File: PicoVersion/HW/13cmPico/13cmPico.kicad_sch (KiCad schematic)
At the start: 70 parts, among them SW1 KEY_1, SW101 RotaryEncoder_Switch, SW102 RESET, SW2 KEY_2, SW3 KEY_3, U1 ADF4351, U101 Pico, U102 LM4562, U103 LM4562, U104 AD8346, U105 LM4562, U2 KT2520K-T

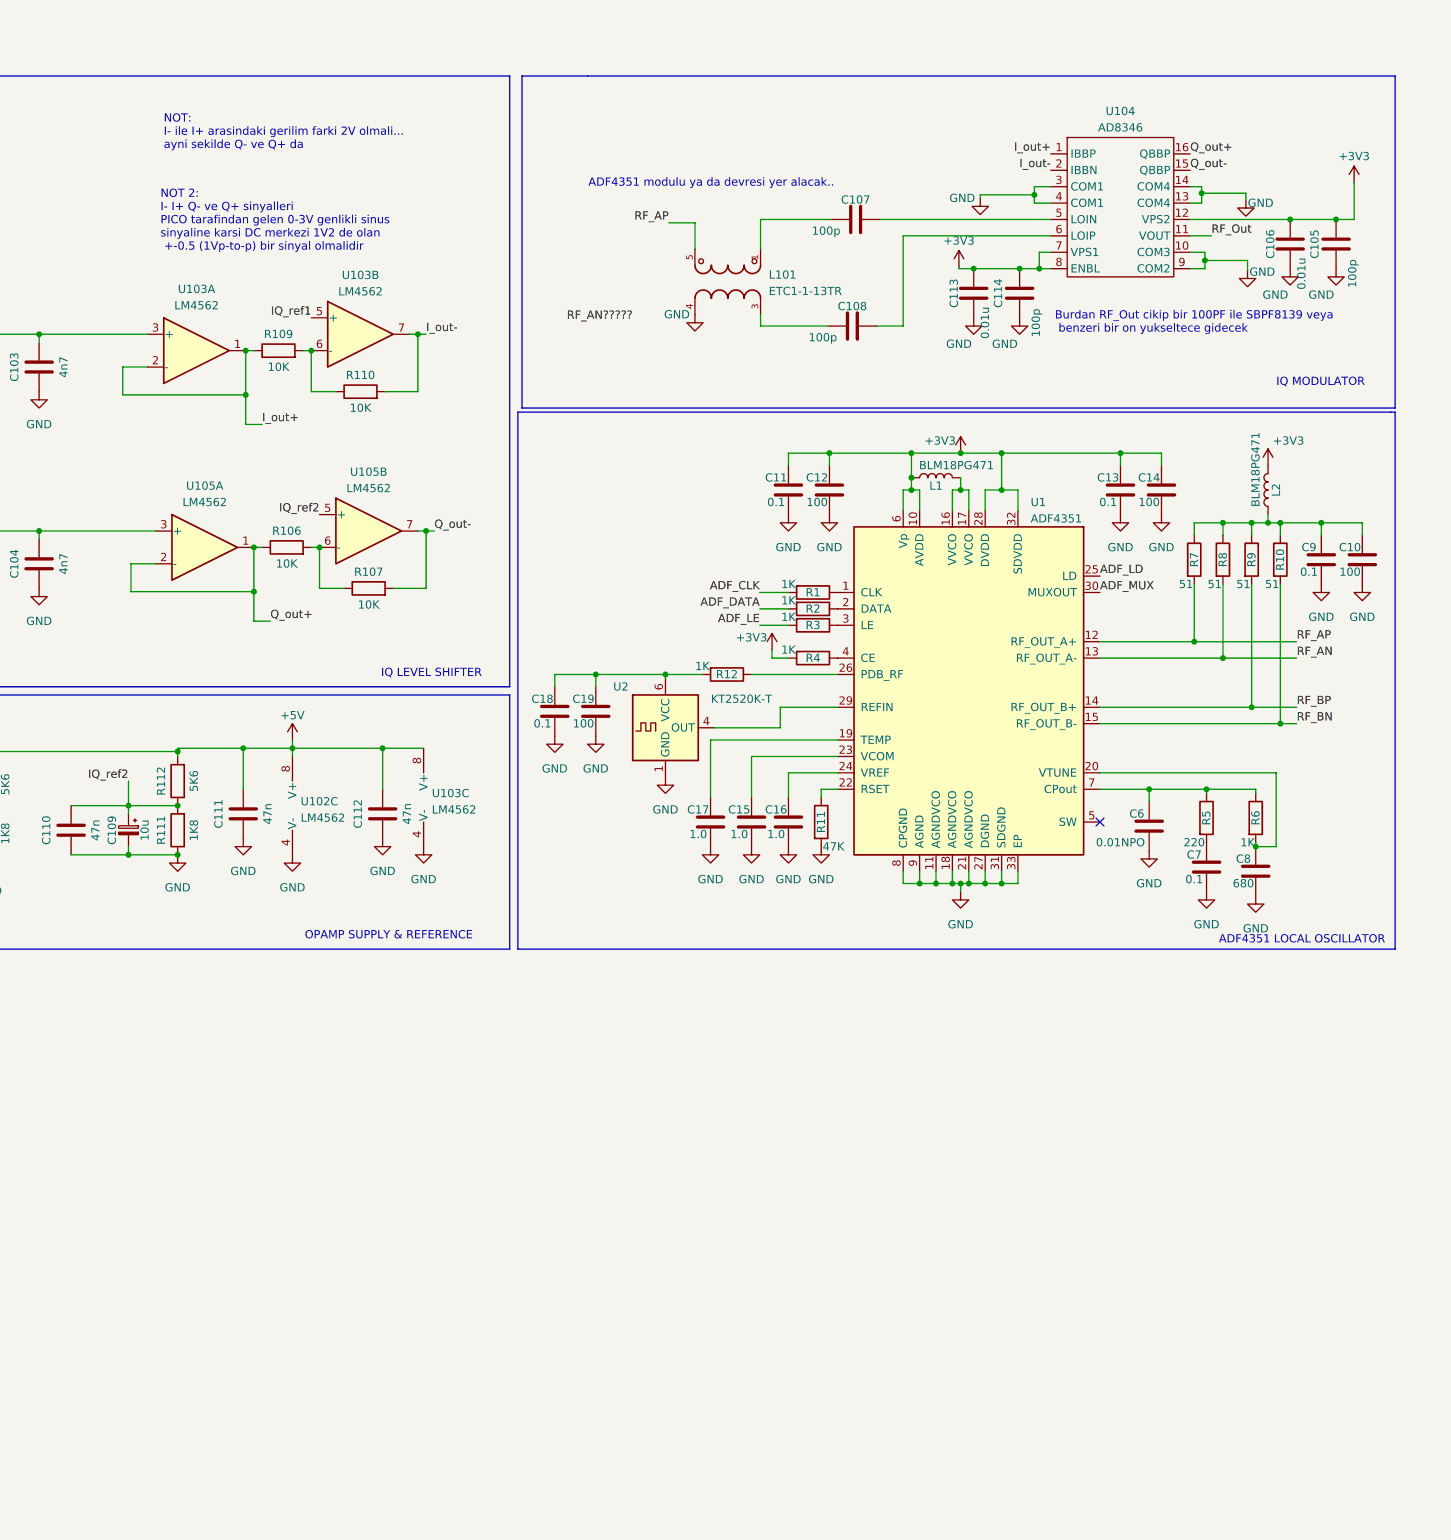
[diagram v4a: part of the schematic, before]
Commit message: ADF435X modules added
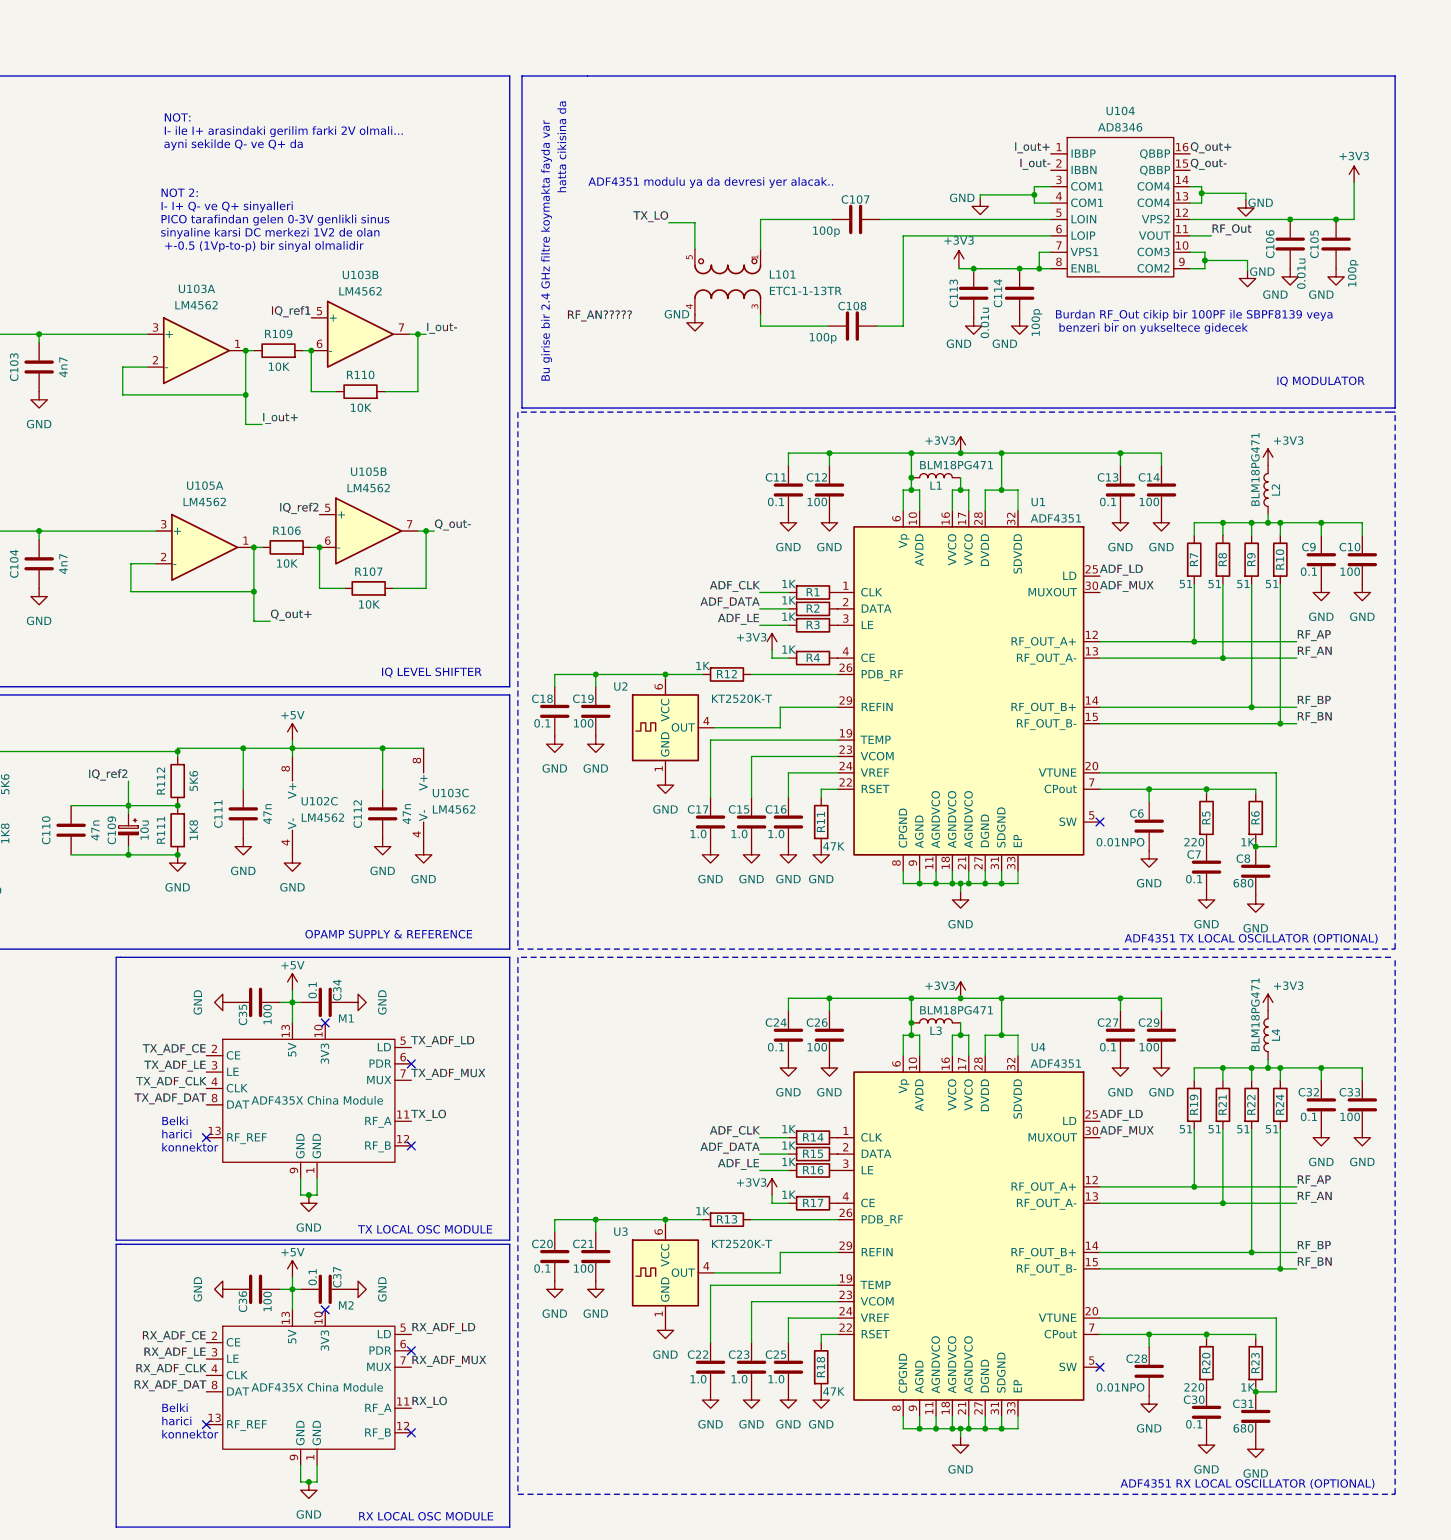
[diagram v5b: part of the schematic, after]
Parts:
- added C20, C24, C27, C30, C32, C34, C37: 0.1, Capacitor_SMD:C_0805_2012Metric, symbol Device:C
- added C21, C26, C29, C33, C35, C36: 100, Capacitor_SMD:C_0805_2012Metric, symbol Device:C
- added C22, C23, C25: 1.0, Capacitor_SMD:C_0805_2012Metric, symbol Device:C
- added C28: 0.01NPO, Capacitor_SMD:C_0805_2012Metric, symbol Device:C
- added C31: 680, Capacitor_SMD:C_0805_2012Metric, symbol Device:C
- added L3, L4: BLM18PG471, symbol Device:L
- added M1, M2: ADF435X China Module, symbol ADF435X_module:ADF435X_China_Module
- added R13, R14, R15, R16, R17, R23: 1K, Resistor_SMD:R_0805_2012Metric, symbol Device:R
- added R18: 47K, Resistor_SMD:R_0805_2012Metric, symbol Device:R
- added R19, R21, R22, R24: 51, Resistor_SMD:R_0805_2012Metric, symbol Device:R
- added R20: 220, Resistor_SMD:R_0805_2012Metric, symbol Device:R
- added U3: KT2520K-T, Oscillator:Oscillator_SMD_Kyocera_2520-6Pin_2.5x2.0mm, symbol Oscillator:KT2520K-T
- added U4: ADF4351, Package_CSP:LFCSP-32-1EP_5x5mm_P0.5mm_EP3.25x3.25mm, symbol Timer_PLL:ADF4351
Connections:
- net +3V3: now also C24.2, C26.2, C27.2, C29.2, L3.1, L4.2, R17.2, U4.10 (AVDD), U4.28 (DVDD), U4.32 (SDVDD), U4.6 (Vp)
- net +5V: now also C34.1, C35.1, C36.1, C37.1, M1.13 (RF_REF), M2.13 (RF_REF)
- net ADF_CLK: now also R14.2
- net ADF_DATA: now also R15.2
- net ADF_LD: now also U4.25 (LD)
- net ADF_LE: now also R16.2
- net ADF_MUX: now also U4.30 (MUXOUT)
- net GND: now also C20.1, C21.1, C22.1, C23.1, C24.1, C25.1, C26.1, C27.1, C28.1, C29.1, C30.1, C31.1, C32.1, C33.1, C34.2, C35.2, C36.2, C37.2, M1.1 (GND), M1.9 (GND), M2.1 (GND), M2.9 (GND), R18.2, U3.1 (GND), U3.3 (GND), U4.11 (AGNDVCO), U4.18 (AGNDVCO), U4.21 (AGNDVCO), U4.27 (DGND), U4.31 (SDGND), U4.33 (EP), U4.8 (CPGND), U4.9 (AGND)
- net RF_AN: now also R21.2, U4.13 (RF_OUT_A-)
- net RF_AP: now also R19.2, U4.12 (RF_OUT_A+); no longer L101.5
- net RF_BN: now also R24.2, U4.15 (RF_OUT_B-)
- net RF_BP: now also R22.2, U4.14 (RF_OUT_B+)
- new net: C23.2, U4.23 (VCOM)
- new net: C20.2, C21.2, R13.2, U3.6 (VCC)
- new net: C32.2, C33.2, L4.1, R19.1, R21.1, R22.1, R24.1
- new net: C28.2, R20.1, R23.1, U4.7 (CPout)
- new net: C22.2, U4.19 (TEMP)
- new net: R17.1, U4.4 (CE)
- new net: C30.2, R20.2
- new net: C31.2, R23.2, U4.20 (VTUNE)
- new net: R15.1, U4.2 (DATA)
- new net: C25.2, U4.24 (VREF)
- new net: L3.2, U4.16 (VVCO), U4.17 (VVCO)
- new net: R16.1, U4.3 (LE)
- new net: R14.1, U4.1 (CLK)
- new net: R18.1, U4.22 (RSET)
- new net: R13.1, U4.26 (PDB_RF)
- new net: U3.4 (OUT), U4.29 (REFIN)
- new net RX_ADF_CE: M2.2 (CE)
- new net RX_ADF_CLK: M2.4 (CLK)
- new net RX_ADF_DAT: M2.8 (DAT)
- new net RX_ADF_LD: M2.5 (LD)
- new net RX_ADF_LE: M2.3 (LE)
- new net RX_ADF_MUX: M2.7 (MUX)
- new net RX_LO: M2.11 (RF_A)
- new net TX_ADF_CE: M1.2 (CE)
- new net TX_ADF_CLK: M1.4 (CLK)
- new net TX_ADF_DAT: M1.8 (DAT)
- new net TX_ADF_LD: M1.5 (LD)
- new net TX_ADF_LE: M1.3 (LE)
- new net TX_ADF_MUX: M1.7 (MUX)
- new net TX_LO: L101.5, M1.11 (RF_A)
- no-connect marks 1 -> 10
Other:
- note added: "ADF4351 RX LOCAL OSCILLATOR (OPTIONAL)"
- note added: "ADF4351 TX LOCAL OSCILLATOR (OPTIONAL)"
- note added: "Belki harici konnektor"
- note added: "Bu girise bir 2.4 GHz filtre koymakta fayda var"
- note added: "RX LOCAL OSC MODULE"
- note added: "TX LOCAL OSC MODULE"
- note added: "hatta cikisina da"
- note removed: "ADF4351 LOCAL OSCILLATOR"
